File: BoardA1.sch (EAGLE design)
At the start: 19 parts, among them J1 LOAD_CELL1X03-PTH, J2 FEMALE 2x3, J3 LOAD_CELL1X03-PTH, J5 LOAD_CELL1X03-PTH, J6 LOAD_CELL1X03-PTH

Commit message: update2
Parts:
- removed J4, J7: (no value), SparkFun-Connectors:M04X2
- added LOADCELL: (no value), SparkFun-Connectors:CONN_04X2
- added LOWERLOADCELL: (no value), SparkFun-Connectors:CONN_05
- added MOTOR: (no value), SparkFun-Connectors:CONN_02
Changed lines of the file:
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@@
 <part name="J6" library="Smartcrutches" deviceset="LOAD_CELL" device="1X03-PTH"/>
 <part name="J2" library="SparkFun-Connectors" deviceset="CONN_03X2" device="FEMALE" value="FEMALE 2x3"/>
-<part name="J4" library="SparkFun-Connectors" deviceset="M04X2" device=""/>
-<part name="J7" library="SparkFun-Connectors" deviceset="M04X2" device=""/>
+<part name="MOTOR" library="SparkFun-Connectors" deviceset="CONN_02" device=""/>
+<part name="LOWERLOADCELL" library="SparkFun-Connectors" deviceset="CONN_05" device=""/>
+<part name="LOADCELL" library="SparkFun-Connectors" deviceset="CONN_04X2" device=""/>
 </parts>
 <sheets>
@@
 <instance part="J6" gate="G$1" x="78.74" y="-33.02"/>
 <instance part="J2" gate="G$1" x="134.62" y="2.54"/>
-<instance part="J4" gate="G$1" x="134.62" y="-25.4"/>
-<instance part="J7" gate="G$1" x="129.54" y="-48.26"/>
+<instance part="MOTOR" gate="G$1" x="116.84" y="-50.8"/>
+<instance part="LOWERLOADCELL" gate="G$1" x="139.7" y="-30.48"/>
+<instance part="LOADCELL" gate="G$1" x="119.38" y="-20.32"/>
 </instances>
 <busses>
@@
 </sheet>
 </sheets>
+<errors>
+</errors>
 </schematic>
 </drawing>

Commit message: update 3
added battery connector
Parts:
- C1, C2, C3, C4: device SparkFun-Capacitors:CAP0805 -> SparkFun-Capacitors:CAPKIT
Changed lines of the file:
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@@
 <grid distance="0.1" unitdist="inch" unit="inch" style="lines" multiple="1" display="no" altdistance="0.01" altunitdist="inch" altunit="inch"/>
 <layers>
-<layer number="1" name="Top" color="4" fill="1" visible="no" active="no"/>
-<layer number="2" name="Route2" color="1" fill="3" visible="no" active="no"/>
-<layer number="3" name="Route3" color="4" fill="3" visible="no" active="no"/>
-<layer number="4" name="Route4" color="1" fill="4" visible="no" active="no"/>
-<layer number="5" name="Route5" color="4" fill="4" visible="no" active="no"/>
-<layer number="6" name="Route6" color="1" fill="8" visible="no" active="no"/>
-<layer number="7" name="Route7" color="4" fill="8" visible="no" active="no"/>
-<layer number="8" name="Route8" color="1" fill="2" visible="no" active="no"/>
-<layer number="9" name="Route9" color="4" fill="2" visible="no" active="no"/>
-<layer number="10" name="Route10" color="1" fill="7" visible="no" active="no"/>
-<layer number="11" name="Route11" color="4" fill="7" visible="no" active="no"/>
-<layer number="12" name="Route12" color="1" fill="5" visible="no" active="no"/>
-<layer number="13" name="Route13" color="4" fill="5" visible="no" active="no"/>
-<layer number="14" name="Route14" color="1" fill="6" visible="no" active="no"/>
-<layer number="15" name="Route15" color="4" fill="6" visible="no" active="no"/>
-<layer number="16" name="Bottom" color="1" fill="1" visible="no" active="no"/>
-<layer number="17" name="Pads" color="2" fill="1" visible="no" active="no"/>
-<layer number="18" name="Vias" color="2" fill="1" visible="no" active="no"/>
-<layer number="19" name="Unrouted" color="6" fill="1" visible="no" active="no"/>
-<layer number="20" name="Dimension" color="15" fill="1" visible="no" active="no"/>
-<layer number="21" name="tPlace" color="7" fill="1" visible="no" active="no"/>
-<layer number="22" name="bPlace" color="7" fill="1" visible="no" active="no"/>
-<layer number="23" name="tOrigins" color="15" fill="1" visible="no" active="no"/>
-<layer number="24" name="bOrigins" color="15" fill="1" visible="no" active="no"/>
-<layer number="25" name="tNames" color="7" fill="1" visible="no" active="no"/>
-<layer number="26" name="bNames" color="7" fill="1" visible="no" active="no"/>
-<layer number="27" name="tValues" color="7" fill="1" visible="no" active="no"/>
-<layer number="28" name="bValues" color="7" fill="1" visible="no" active="no"/>
+<layer number="1" name="Top" color="4" fill="1" visible="yes" active="no"/>
+<layer number="2" name="Route2" color="1" fill="3" visible="yes" active="no"/>
+<layer number="3" name="Route3" color="4" fill="3" visible="yes" active="no"/>
+<layer number="4" name="Route4" color="1" fill="4" visible="yes" active="no"/>
+<layer number="5" name="Route5" color="4" fill="4" visible="yes" active="no"/>
+<layer number="6" name="Route6" color="1" fill="8" visible="yes" active="no"/>
+<layer number="7" name="Route7" color="4" fill="8" visible="yes" active="no"/>
+<layer number="8" name="Route8" color="1" fill="2" visible="yes" active="no"/>
+<layer number="9" name="Route9" color="4" fill="2" visible="yes" active="no"/>
+<layer number="10" name="Route10" color="1" fill="7" visible="yes" active="no"/>
+<layer number="11" name="Route11" color="4" fill="7" visible="yes" active="no"/>
+<layer number="12" name="Route12" color="1" fill="5" visible="yes" active="no"/>
+<layer number="13" name="Route13" color="4" fill="5" visible="yes" active="no"/>
+<layer number="14" name="Route14" color="1" fill="6" visible="yes" active="no"/>
+<layer number="15" name="Route15" color="4" fill="6" visible="yes" active="no"/>
+<layer number="16" name="Bottom" color="1" fill="1" visible="yes" active="no"/>
+<layer number="17" name="Pads" color="2" fill="1" visible="yes" active="no"/>
+<layer number="18" name="Vias" color="2" fill="1" visible="yes" active="no"/>
+<layer number="19" name="Unrouted" color="6" fill="1" visible="yes" active="no"/>
+<layer number="20" name="Dimension" color="15" fill="1" visible="yes" active="no"/>
+<layer number="21" name="tPlace" color="7" fill="1" visible="yes" active="no"/>
+<layer number="22" name="bPlace" color="7" fill="1" visible="yes" active="no"/>
+<layer number="23" name="tOrigins" color="15" fill="1" visible="yes" active="no"/>
+<layer number="24" name="bOrigins" color="15" fill="1" visible="yes" active="no"/>
+<layer number="25" name="tNames" color="7" fill="1" visible="yes" active="no"/>
+<layer number="26" name="bNames" color="7" fill="1" visible="yes" active="no"/>
+<layer number="27" name="tValues" color="7" fill="1" visible="yes" active="no"/>
+<layer number="28" name="bValues" color="7" fill="1" visible="yes" active="no"/>
 <layer number="29" name="tStop" color="7" fill="3" visible="no" active="no"/>
 <layer number="30" name="bStop" color="7" fill="6" visible="no" active="no"/>
@@
 <layer number="35" name="tGlue" color="7" fill="4" visible="no" active="no"/>
 <layer number="36" name="bGlue" color="7" fill="5" visible="no" active="no"/>
-<layer number="37" name="tTest" color="7" fill="1" visible="no" active="no"/>
-<layer number="38" name="bTest" color="7" fill="1" visible="no" active="no"/>
+<layer number="37" name="tTest" color="7" fill="1" visible="yes" active="no"/>
+<layer number="38" name="bTest" color="7" fill="1" visible="yes" active="no"/>
 <layer number="39" name="tKeepout" color="4" fill="11" visible="no" active="no"/>
 <layer number="40" name="bKeepout" color="1" fill="11" visible="no" active="no"/>
@@
 <layer number="44" name="Drills" color="7" fill="1" visible="no" active="no"/>
 <layer number="45" name="Holes" color="7" fill="1" visible="no" active="no"/>
-<layer number="46" name="Milling" color="3" fill="1" visible="no" active="no"/>
-<layer number="47" name="Measures" color="7" fill="1" visible="no" active="no"/>
-<layer number="48" name="Document" color="7" fill="1" visible="no" active="no"/>
-<layer number="49" name="Reference" color="7" fill="1" visible="no" active="no"/>
-<layer number="50" name="dxf" color="7" fill="1" visible="no" active="no"/>
-<layer number="51" name="tDocu" color="9" fill="1" visible="no" active="no"/>
-<layer number="52" name="bDocu" color="7" fill="1" visible="no" active="no"/>
-<layer number="53" name="tGND_GNDA" color="7" fill="9" visible="no" active="no"/>
-<layer number="54" name="bGND_GNDA" color="1" fill="9" visible="no" active="no"/>
-<layer number="56" name="wert" color="7" fill="1" visible="no" active="no"/>
-<layer number="57" name="tCAD" color="7" fill="1" visible="no" active="no"/>
-<layer number="59" name="tCarbon" color="7" fill="1" visible="no" active="no"/>
-<layer number="60" name="bCarbon" color="7" fill="1" visible="no" active="no"/>
+<layer number="46" name="Milling" color="3" fill="1" visible="yes" active="no"/>
+<layer number="47" name="Measures" color="7" fill="1" visible="yes" active="no"/>
+<layer number="48" name="Document" color="7" fill="1" visible="yes" active="no"/>
+<layer number="49" name="Reference" color="7" fill="1" visible="yes" active="no"/>
+<layer number="50" name="dxf" color="7" fill="1" visible="yes" active="no"/>
+<layer number="51" name="tDocu" color="9" fill="1" visible="yes" active="no"/>
+<layer number="52" name="bDocu" color="7" fill="1" visible="yes" active="no"/>
+<layer number="53" name="tGND_GNDA" color="7" fill="9" visible="yes" active="no"/>
+<layer number="54" name="bGND_GNDA" color="1" fill="9" visible="yes" active="no"/>
+<layer number="56" name="wert" color="7" fill="1" visible="yes" active="no"/>
+<layer number="57" name="tCAD" color="7" fill="1" visible="yes" active="no"/>
+<layer number="59" name="tCarbon" color="7" fill="1" visible="yes" active="no"/>
+<layer number="60" name="bCarbon" color="7" fill="1" visible="yes" active="no"/>
 <layer number="90" name="Modules" color="5" fill="1" visible="yes" active="yes"/>
 <layer number="91" name="Nets" color="2" fill="1" visible="yes" active="yes"/>
@@
 <parts>
 <part name="U$1" library="Smartcrutches" deviceset="DC-DC" device=""/>
-<part name="C1" library="SparkFun-Capacitors" deviceset="CAP" device="0805"/>
+<part name="C1" library="SparkFun-Capacitors" deviceset="CAP" device="KIT"/>
 <part name="S1" library="SparkFun-Electromechanical" deviceset="SWITCH-SPDT" device="PTH"/>
-<part name="C2" library="SparkFun-Capacitors" deviceset="CAP" device="0805"/>
-<part name="C3" library="SparkFun-Capacitors" deviceset="CAP" device="0805"/>
-<part name="C4" library="SparkFun-Capacitors" deviceset="CAP" device="0805"/>
+<part name="C2" library="SparkFun-Capacitors" deviceset="CAP" device="KIT"/>
+<part name="C3" library="SparkFun-Capacitors" deviceset="CAP" device="KIT"/>
+<part name="C4" library="SparkFun-Capacitors" deviceset="CAP" device="KIT"/>
 <part name="U$2" library="Smartcrutches" deviceset="ICA3H" device=""/>
 <part name="J1" library="Smartcrutches" deviceset="LOAD_CELL" device="1X03-PTH"/>

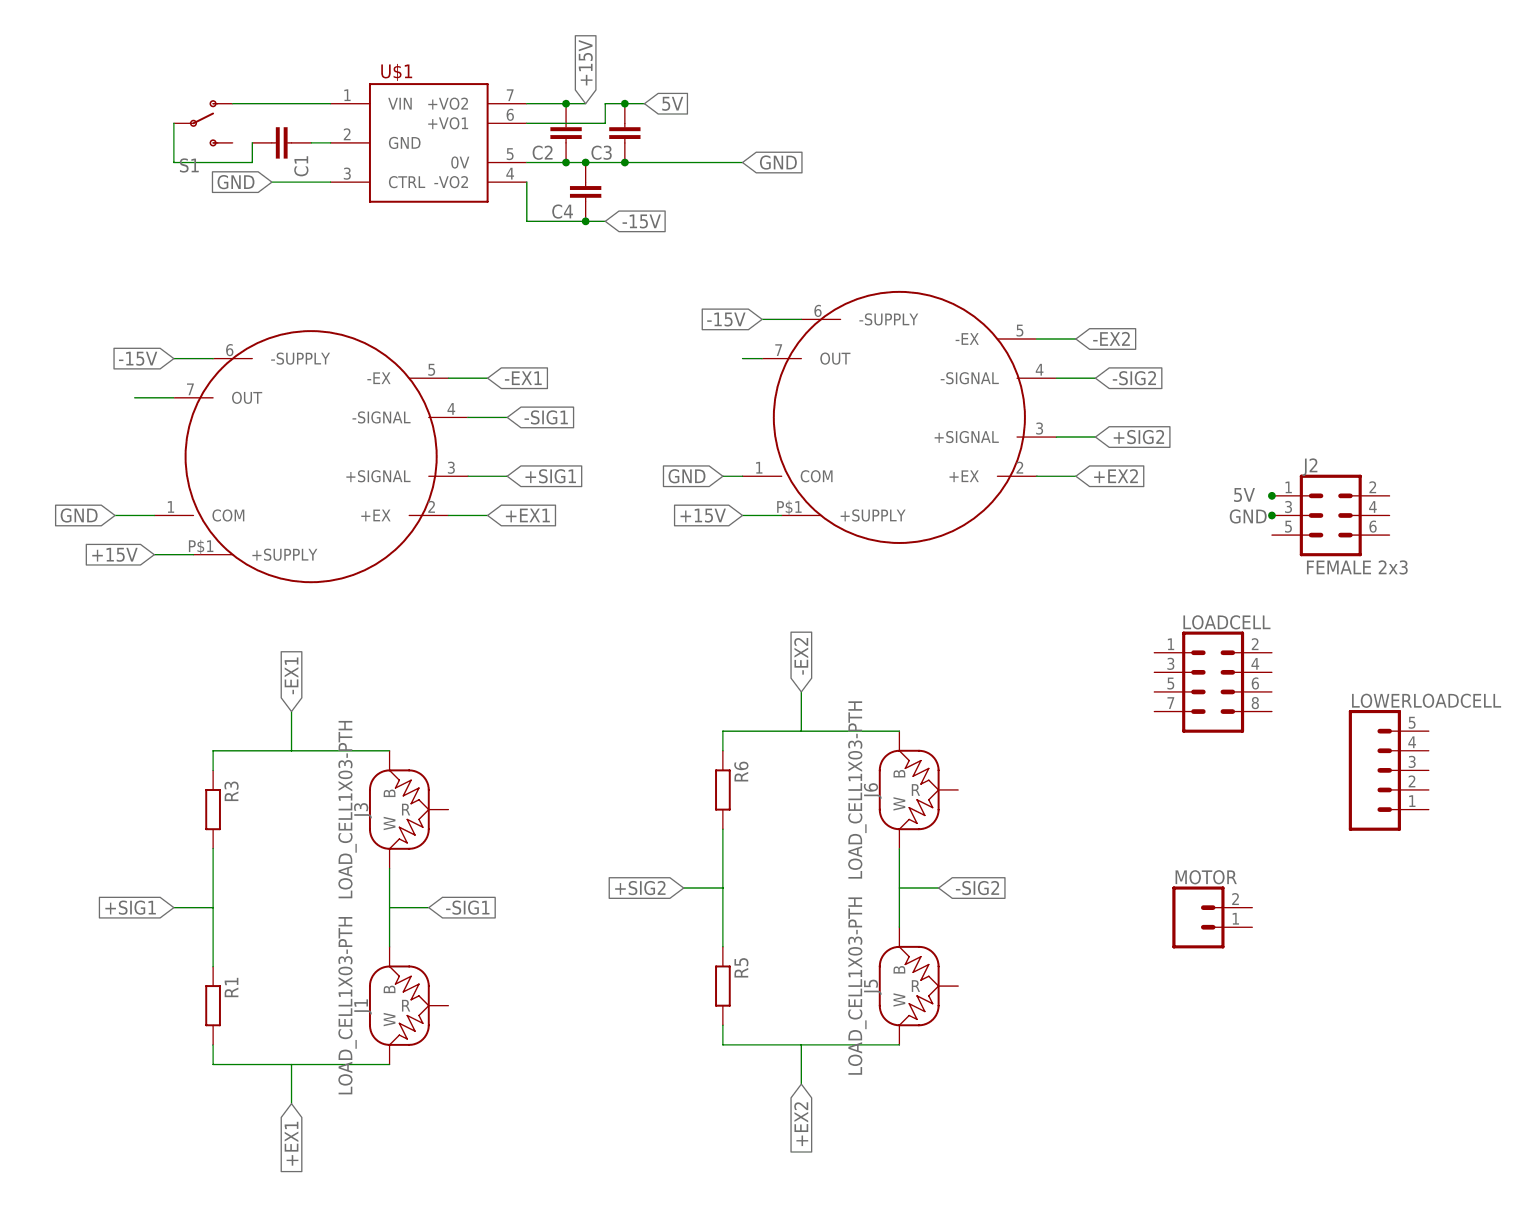
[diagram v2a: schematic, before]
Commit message: moved motor connector
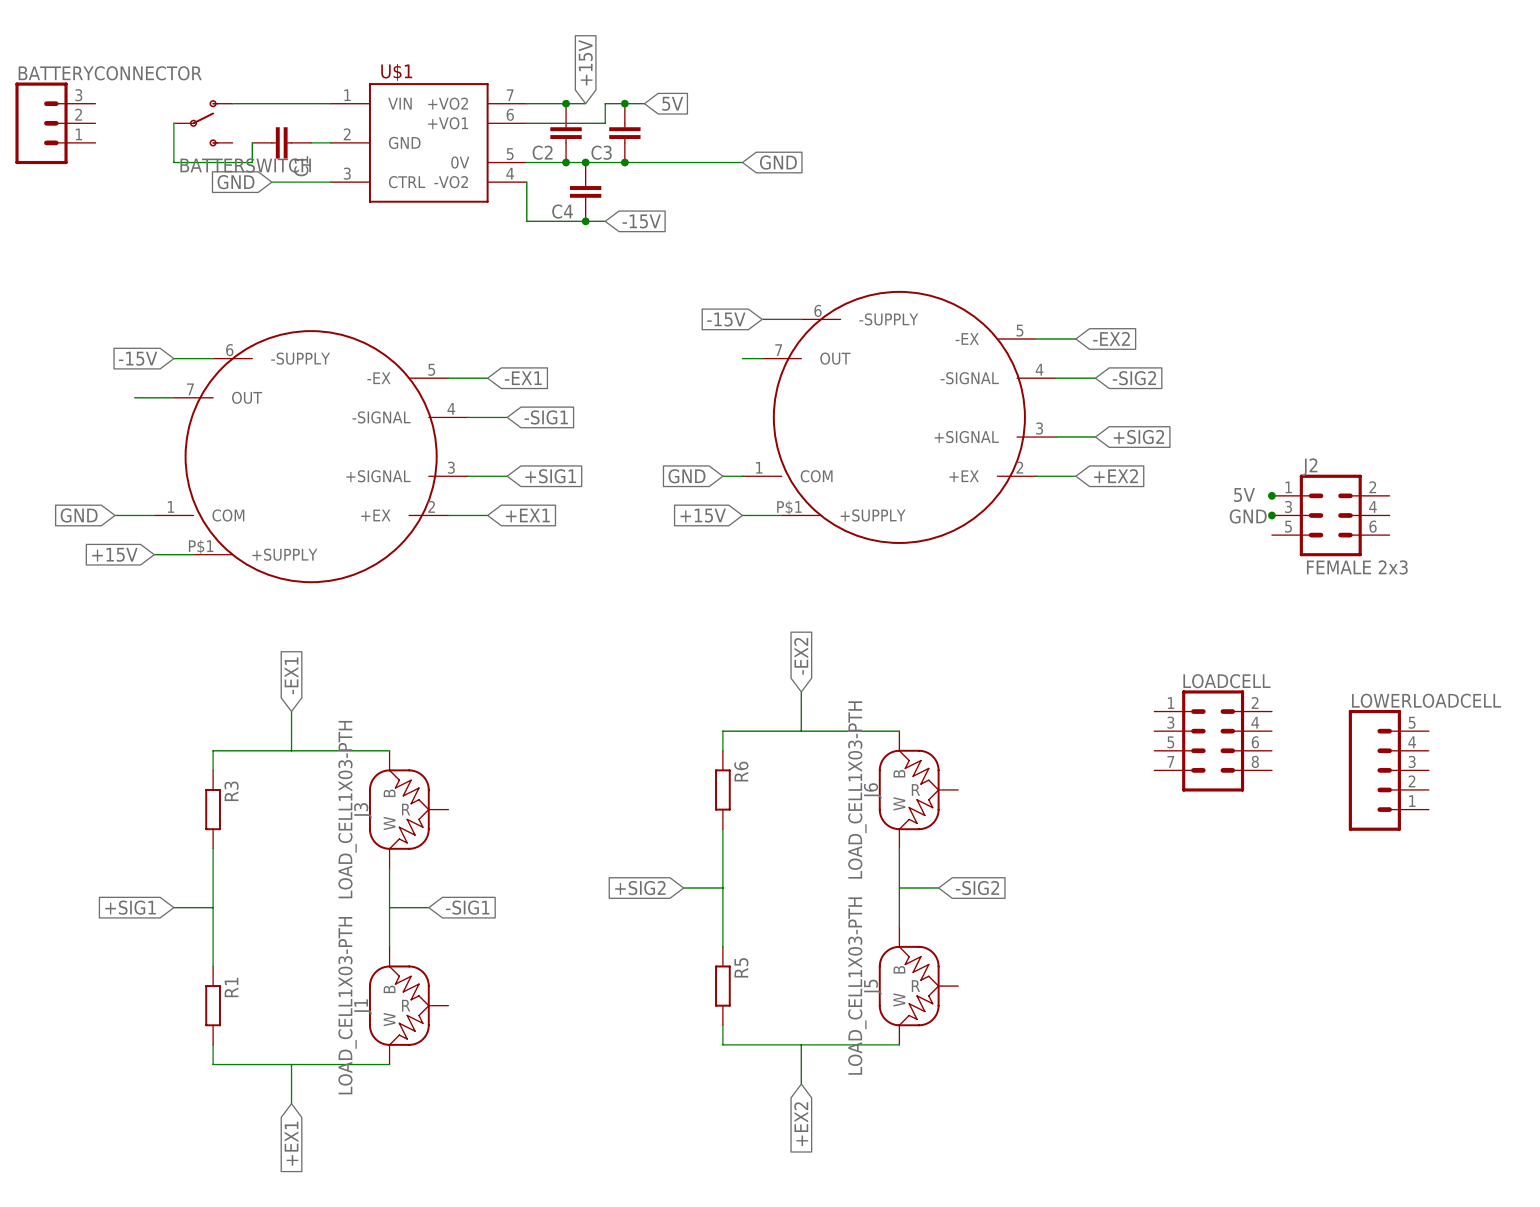
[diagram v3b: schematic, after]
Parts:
- removed MOTOR: (no value), SparkFun-Connectors:CONN_02
- added BATTERYCONNECTOR: (no value), SparkFun-Connectors:CONN_03LOCK
- renumbered S1 to BATTERSWITCH
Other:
- moved on the sheet: LOADCELL

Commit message: Teensy Pin Update2
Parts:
- removed LOWERLOADCELL: (no value), SparkFun-Connectors:CONN_05
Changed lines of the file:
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@@
 <part name="J6" library="Smartcrutches" deviceset="LOAD_CELL" device="1X03-PTH"/>
 <part name="J2" library="SparkFun-Connectors" deviceset="CONN_03X2" device="FEMALE" value="FEMALE 2x3"/>
-<part name="LOWERLOADCELL" library="SparkFun-Connectors" deviceset="CONN_05" device=""/>
 <part name="LOADCELL" library="SparkFun-Connectors" deviceset="CONN_04X2" device=""/>
 <part name="BATTERYCONNECTOR" library="SparkFun-Connectors" deviceset="CONN_03" device="LOCK"/>
@@
 <instance part="J6" gate="G$1" x="78.74" y="-33.02"/>
 <instance part="J2" gate="G$1" x="134.62" y="2.54"/>
-<instance part="LOWERLOADCELL" gate="G$1" x="139.7" y="-30.48"/>
 <instance part="LOADCELL" gate="G$1" x="119.38" y="-27.94"/>
 <instance part="BATTERYCONNECTOR" gate="J$1" x="-33.02" y="53.34"/>
